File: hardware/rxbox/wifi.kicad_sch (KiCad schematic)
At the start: 1 part, among them U9 RTL8723DS

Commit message: sdio bus + new wifi module
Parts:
- removed U9: RTL8723DS, Package_DFN_QFN:QFN-48-1EP_6x6mm_P0.4mm_EP4.2x4.2mm_ThermalVias, symbol RF_WiFi_Custom:RTL8723DS
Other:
- note removed: "0:SMPS / 1:LDO"

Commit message: wifi updates
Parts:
- added AE1: Antenna_Shield, symbol Device:Antenna_Shield
- added C22, C33: 100nF, symbol Device:C_Small
- added C23, C29: 10uF, symbol Device:C_Small
- added C27, C28: 16pF, symbol Device:C_Small
- added C30, C31, C32: 22pF, symbol Device:C_Small
- added J1: Uf.C, Connector_Coaxial:U.FL_Molex_MCRF_73412-0110_Vertical, symbol Connector:Conn_Coaxial_Small
- added L7: 2.2uH, symbol Device:L_Small
- added U11: PE4259, Package_TO_SOT_SMD:SOT-363_SC-70-6, symbol RF_Switch_Custom:PE4259
- added U9: AP6212, symbol RF_WiFi_Custom:AP6212
- added Y1: 26MHz, symbol Device:Crystal_GND24_Small
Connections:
- new net: C31.2, U11.1 (RF1)
- new net: C32.2, U11.3 (RF2)
- new net: C30.1, U11.5 (RFC)
- new net: C32.1, J1.1 (In)
- new net: C27.1, U9.10 (XTAL_IN), Y1.3
- new net: L7.1, U9.21 (VIN_LDO_OUT)
- new net: C29.1, L7.2, U9.23 (VIN_LDO)
- new net: C28.1, U9.11 (XTAL_OUT), Y1.1
- new net: U9.29 (NC), U9.30 (NC), U9.32 (NC), U9.35 (NC), U9.37 (NC), U9.38 (NC), U9.47 (NC), U9.5 (NC), U9.8 (NC)
- new net: AE1.1 (A), C31.1
- new net 32KHZ: U9.24 (LPO)
- new net BT_HOST_WAKE: U9.7 (BT_HOST_WAKE)
- new net BT_RST_N: U9.34 (BT_RST_N)
- new net BT_WAKE: U9.6 (BT_WAKE)
- new net Earth: AE1.2 (Shield), C22.2, C23.1, C27.2, C28.2, C29.2, C33.2, J1.2 (Ext), U11.2 (GND), U9.1 (GND), U9.20 (GND), U9.3 (GND), U9.31 (GND), U9.33 (GND), U9.36 (GND), Y1.2 (G), Y1.4 (G)
- new net WIFI.CLK: U9.17 (SDIO_DATA_CLK)
- new net WIFI.CMD: U9.16 (SDIO_DATA_CMD)
- new net WIFI.CTS: U9.44 (UART_CTS_N)
- new net WIFI.D0: U9.18 (SDIO_DATA_0)
- new net WIFI.D1: U9.19 (SDIO_DATA_1)
- new net WIFI.D2: U9.14 (SDIO_DATA_2)
- new net WIFI.D3: U9.15 (SDIO_DATA_3)
- new net WIFI.RTS: U9.41 (UART_RTS_N)
- new net WIFI.RXD: U9.43 (UART_RXD)
- new net WIFI.TXD: U9.42 (UART_TXD)
- new net WIFI_3V3: C22.1, C23.2, C33.1, U11.6 (VDD), U9.22 (VDDIO), U9.9 (VBAT)
- new net WL_BT_ANT: C30.2, U9.2 (WL_BT_ANT)
- new net WL_HOST_WAKE: U9.13 (WL_HOST_WAKE)
- new net WL_REG_ON: U9.12 (WL_REG_ON)
- no-connect marks 0 -> 9
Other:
- note added: "RF PATH 2.4 GHZ"

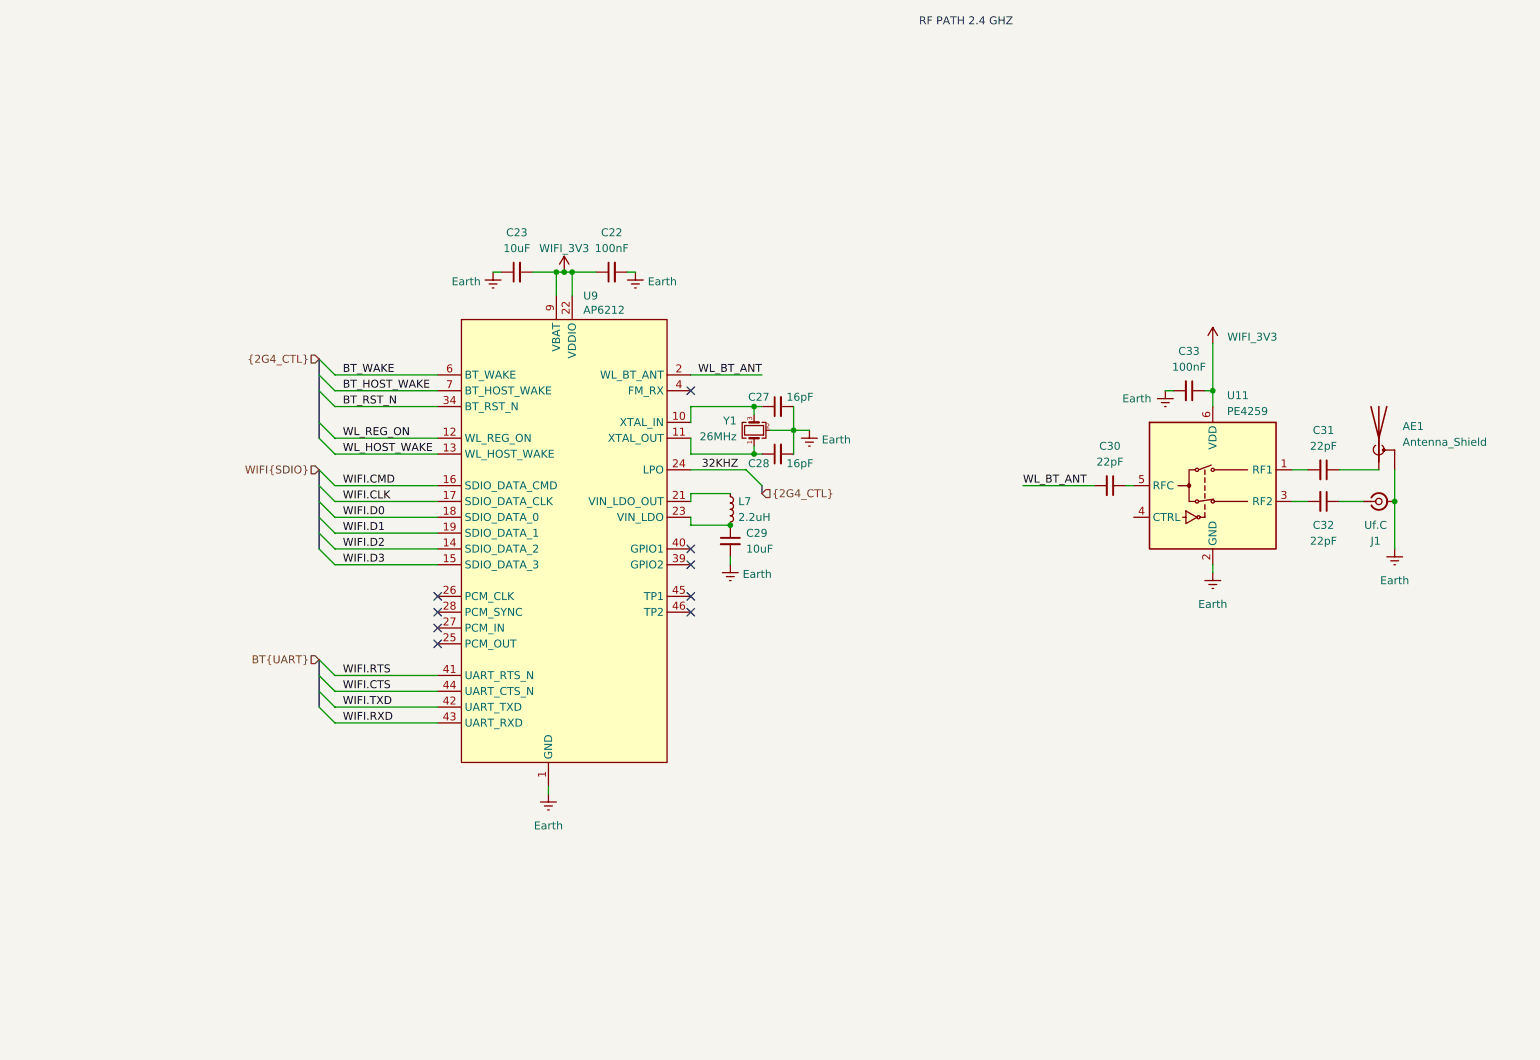
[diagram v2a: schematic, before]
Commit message: wiring wifi + bt to t113
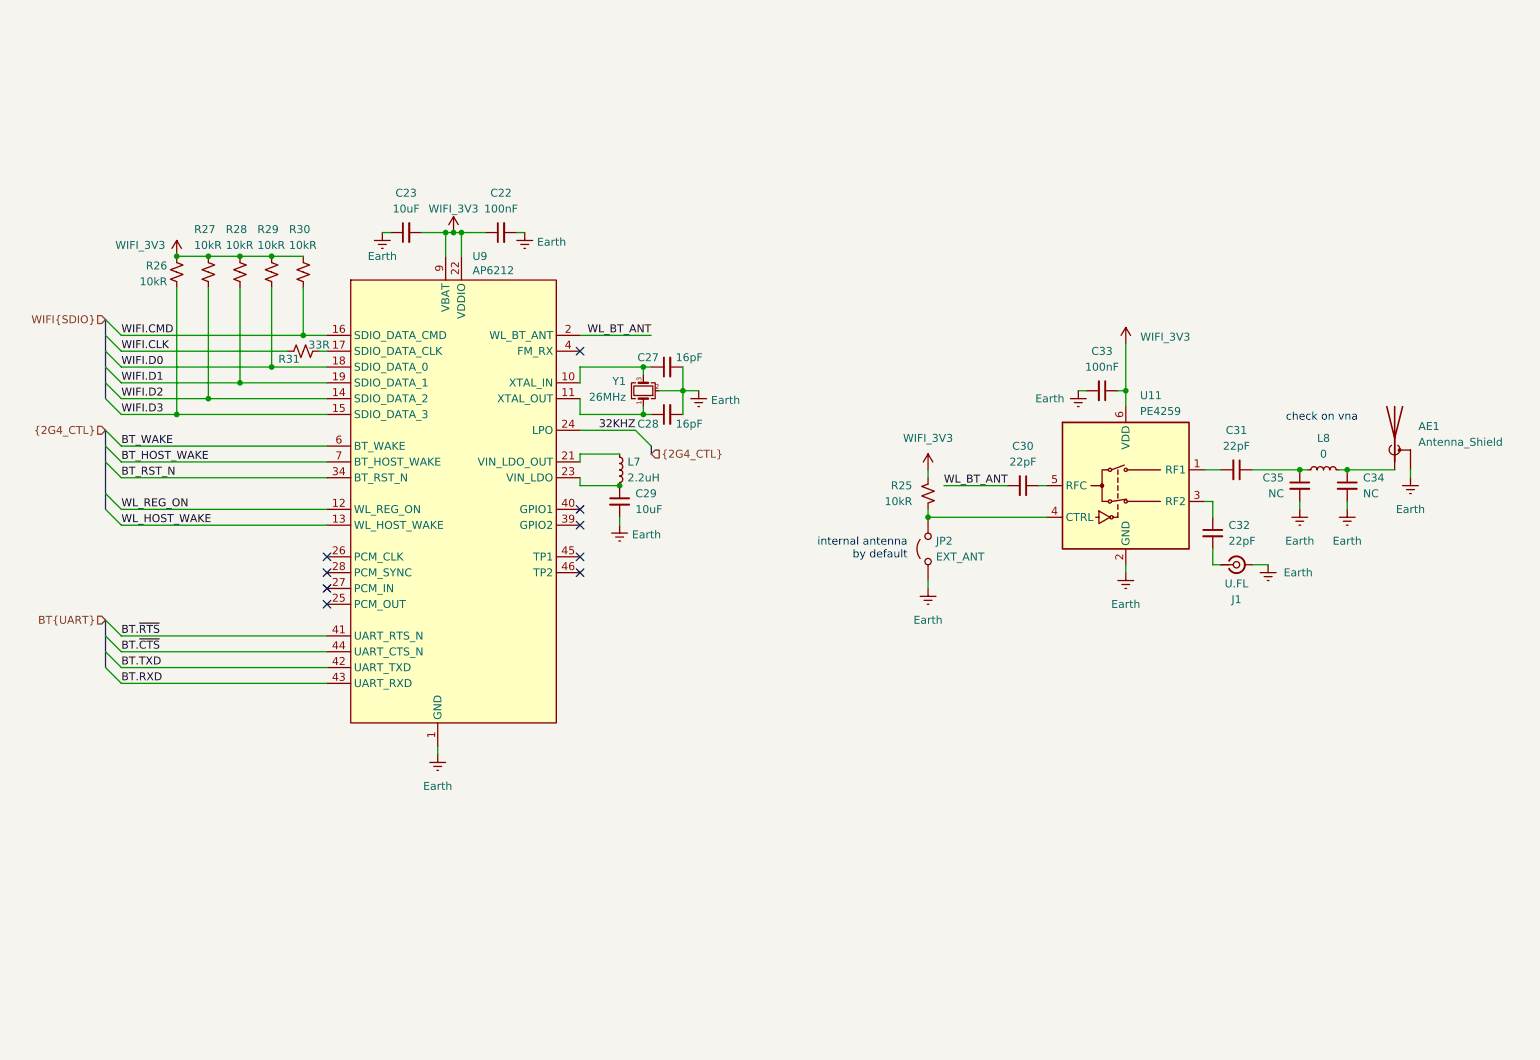
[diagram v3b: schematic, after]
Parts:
- added C34, C35: NC, symbol Device:C_Small
- added JP2: EXT_ANT, symbol Jumper:Jumper_2_Open
- added L8: 0, symbol Device:L_Small
- added R25, R26, R27, R28, R29, R30: 10kR, symbol Device:R_Small_US
- added R31: 33R, symbol Device:R_Small_US
- J1: value Uf.C -> U.FL
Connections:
- net Earth: now also C34.2, C35.2, JP2.1 (A)
- net WIFI.CLK: now also R31.1; no longer U9.17 (SDIO_DATA_CLK)
- net WIFI.CMD: now also R30.2
- net WIFI.D0: now also R29.2
- net WIFI.D1: now also R28.2
- net WIFI.D2: now also R27.2
- net WIFI.D3: now also R26.2
- net WIFI_3V3: now also R25.1, R26.1, R27.1, R28.1, R29.1, R30.1
- net at U11.3 (RF2): now also C32.1; no longer C32.2
- net at U11.4 (CTRL): now also JP2.2 (B), R25.2
- net at J1.1 (In): now also C32.2; no longer C32.1
- net at C31.1: now also C35.1, L8.1; no longer AE1.1 (A)
- net WIFI.CTS renamed BT.~{CTS}
- net WIFI.RTS renamed BT.~{RTS}
- net WIFI.RXD renamed BT.RXD
- net WIFI.TXD renamed BT.TXD
- new net: R31.2, U9.17 (SDIO_DATA_CLK)
- new net: AE1.1 (A), C34.1, L8.2
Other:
- note added: "check on vna"
- note added: "internal antenna by default"
- note removed: "RF PATH 2.4 GHZ"
- moved on the sheet: AE1, C22, C23, C27, C28, C29, C30, C31, C33, J1, L7, U11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

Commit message: finish hooking up wifi+bt, and power
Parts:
- added R42, R43, R44, R45, R46: 10kR, symbol Device:R_Small_US
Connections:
- net BT_HOST_WAKE: now also R46.2
- net BT_RST_N: now also R43.1
- net BT_WAKE: now also R44.2
- net Earth: now also R42.1, R44.1, R45.1, R46.1
- net WIFI_3V3: now also R25.2, R43.2; no longer R25.1
- net WL_HOST_WAKE: now also R45.2
- net WL_REG_ON: now also R42.2
- net at JP2.2 (B), U11.4 (CTRL): now also R25.1; no longer R25.2
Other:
- note added: "high-impedance on boot"
- moved on the sheet: R25
